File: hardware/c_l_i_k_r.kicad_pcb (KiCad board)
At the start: 2 copper layers, 100 x 100 mm, 45 parts, among them J1 mono_jack_3.5mm, J2 mono_jack_3.5mm, J3 mono_jack_3.5mm, J4 mono_jack_3.5mm, SW1 Push, SW10 Push, SW11 Push, SW12 Push, SW13 Push, SW14 Push, SW15 Push, SW16 Push, SW17 Push, SW18 Push, SW19 Push, SW2 Push, SW20 Push, SW3 Push, SW4 Push, SW5 Push, SW6 Push, SW7 Push, SW8 Push, SW9 Push, U1 ProMicro

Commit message: update bom
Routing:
- net key_y3: track 146.4 -> 147.2 mm
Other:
- board text added: "JLCJLCJLCJLC"

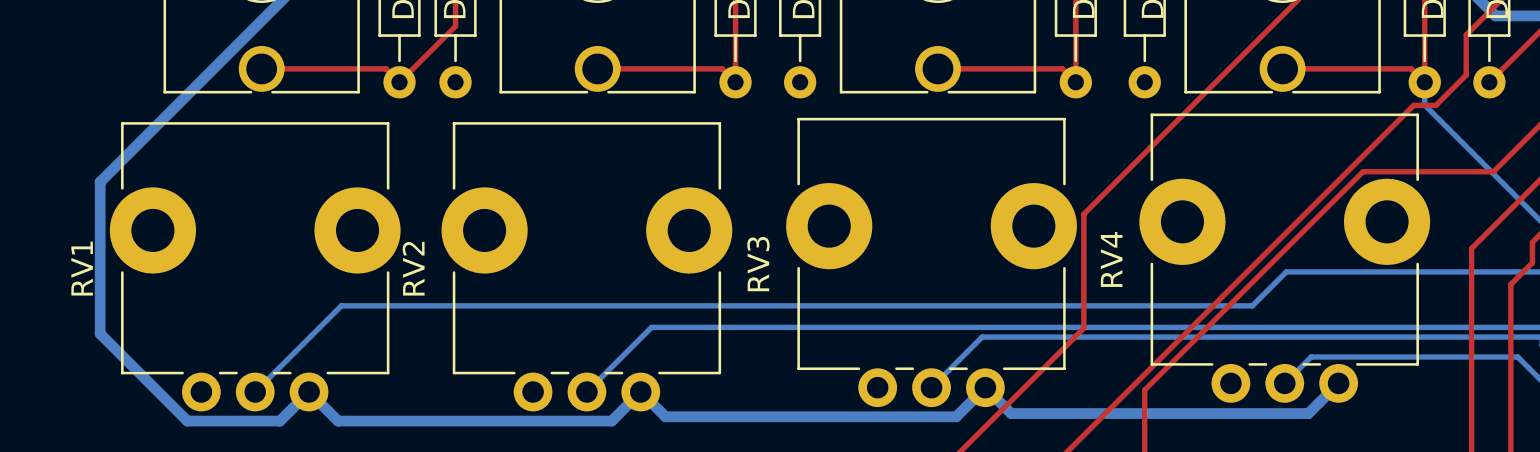
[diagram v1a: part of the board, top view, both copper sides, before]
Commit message: made pot holes larger
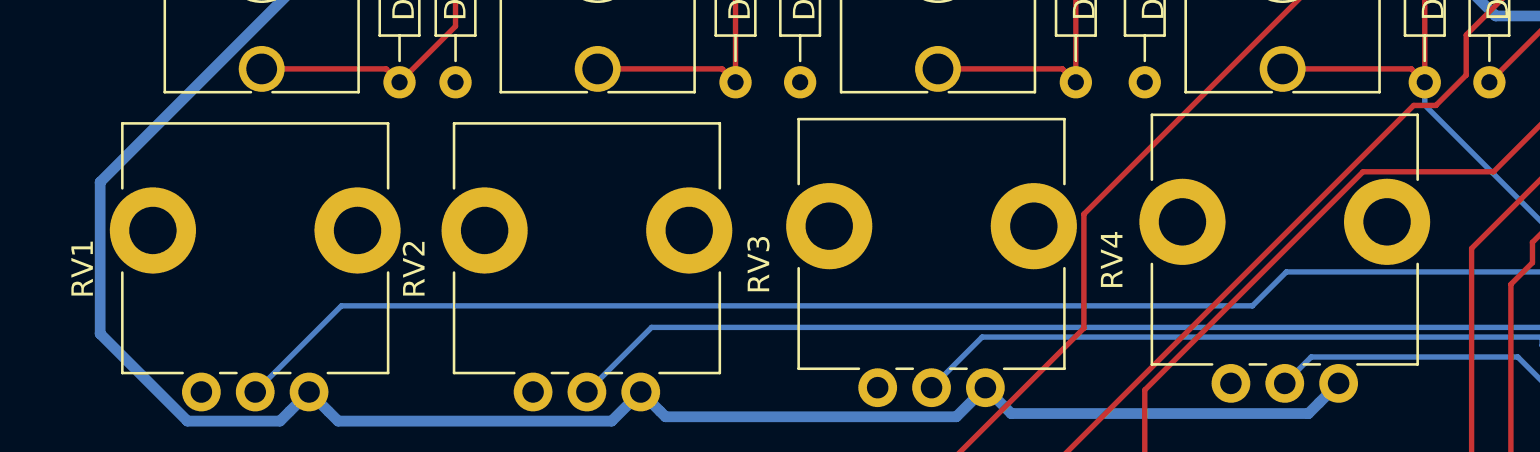
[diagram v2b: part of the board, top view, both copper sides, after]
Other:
- net class Default removed
